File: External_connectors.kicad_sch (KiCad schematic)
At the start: 16 parts, among them CN1 JST_Battery, J11 CAN_TX, J12 CAN_RX, J13 Conn_01x08, J14 Conn_01x06, J15 Conn_01x10, J16 Conn_01x08, J2 A - B, J21 U2U, J3 H - L, J4 TYPE-C-31-M12_13, J5 EXT_LOAD, J9 Conn_01x06

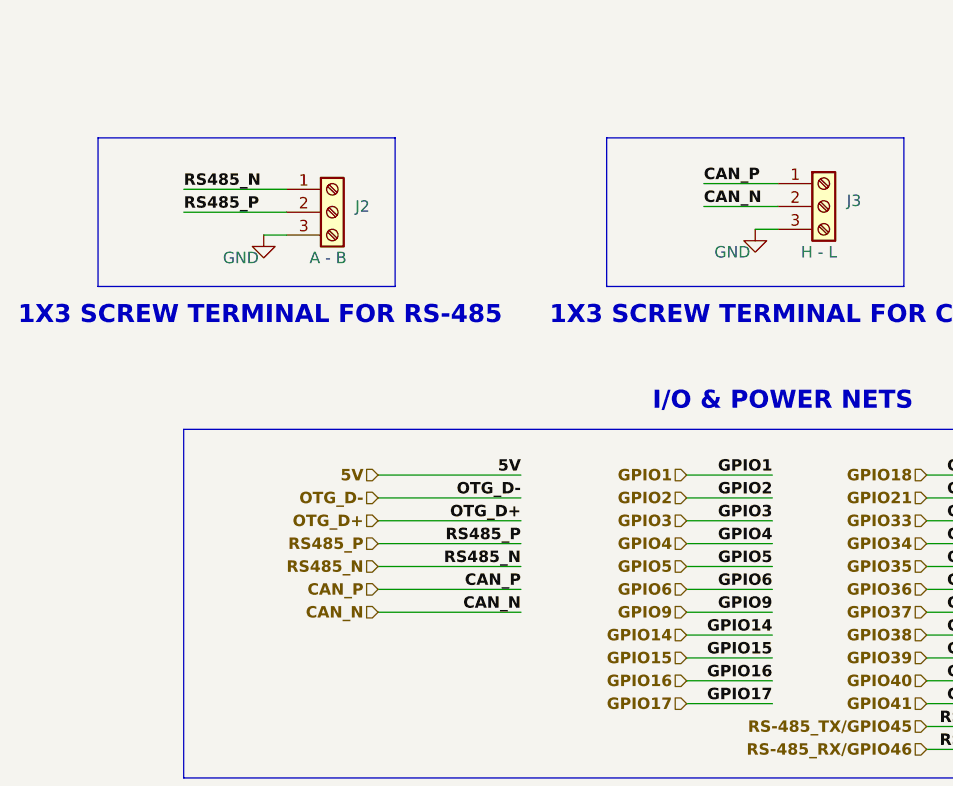
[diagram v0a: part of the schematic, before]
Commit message: Changed GPIO mapping
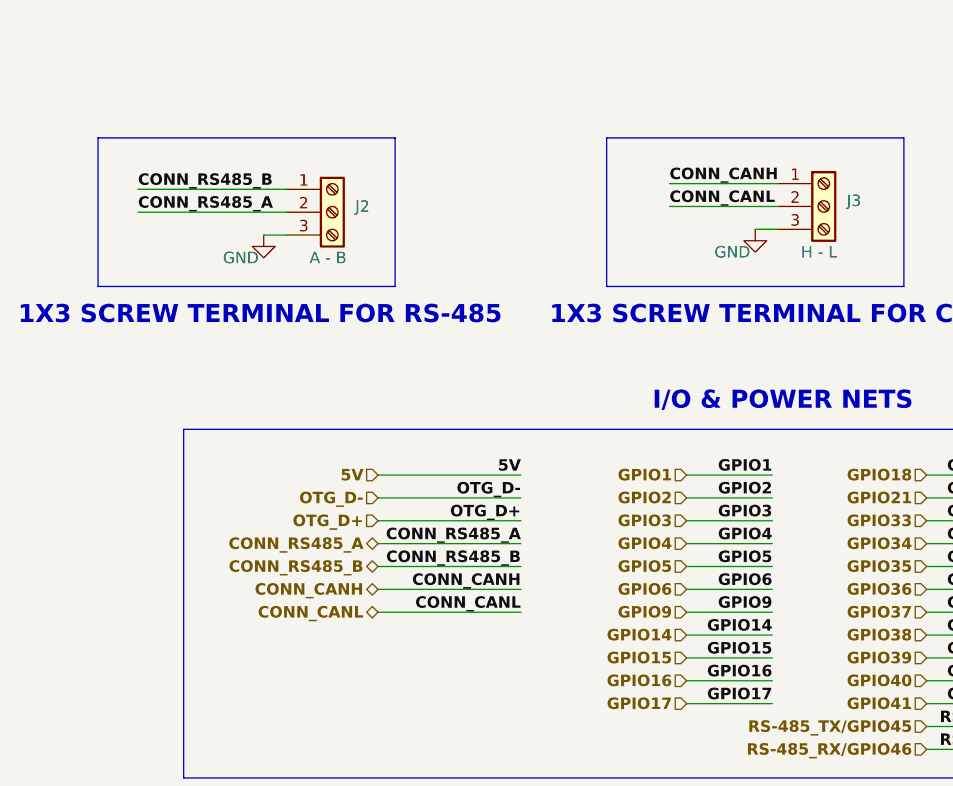
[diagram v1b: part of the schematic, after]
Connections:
- net CAN_N renamed CONN_CANL
- net CAN_P renamed CONN_CANH
- net RS485_N renamed CONN_RS485_B
- net RS485_P renamed CONN_RS485_A
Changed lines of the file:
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@@
     (stroke (width 1) (type default) (color 72 72 72 1))
   )
-  (wire (pts (xy 31.75 132.08) (xy 43.18 132.08))
+  (wire (pts (xy 26.67 132.08) (xy 43.18 132.08))
     (stroke (width 0) (type default))
   )
@@
     (stroke (width 0) (type default))
   )
-  (wire (pts (xy 31.75 129.54) (xy 43.18 129.54))
+  (wire (pts (xy 26.67 129.54) (xy 43.18 129.54))
     (stroke (width 0) (type default))
   )
@@
     (stroke (width 0) (type default))
   )
-  (wire (pts (xy 89.535 128.905) (xy 97.79 128.905))
+  (wire (pts (xy 85.725 128.905) (xy 97.79 128.905))
     (stroke (width 0) (type default))
   )
@@
     (stroke (width 0) (type default))
   )
-  (wire (pts (xy 89.535 131.445) (xy 97.79 131.445))
+  (wire (pts (xy 85.725 131.445) (xy 97.79 131.445))
     (stroke (width 0) (type default))
   )
@@
     (effects (font (size 1.27 1.27) bold (color 72 0 0 1)) (justify right bottom))
   )
-  (label "CAN_P" (at 89.535 128.905 0) (fields_autoplaced)
-    (effects (font (size 1.27 1.27) bold (color 0 0 0 1)) (justify left bottom))
-  )
   (label "V_BAT" (at 250.19 92.075 0) (fields_autoplaced)
     (effects (font (size 1.27 1.27) bold (color 132 132 0 1)) (justify left bottom))
@@
     (effects (font (size 1.27 1.27) bold (color 0 0 255 1)) (justify left bottom))
   )
-  (label "RS485_N" (at 69.215 171.45 180) (fields_autoplaced)
-    (effects (font (size 1.27 1.27) bold (color 0 0 0 1)) (justify right bottom))
-  )
   (label "GPIO4" (at 127 76.835 0) (fields_autoplaced)
     (effects (font (size 1.27 1.27) bold (color 72 0 0 1)) (justify left bottom))
@@
     (effects (font (size 1.27 1.27) bold (color 0 0 255 1)) (justify left bottom))
   )
-  (label "RS485_P" (at 31.75 132.08 0) (fields_autoplaced)
+  (label "CONN_RS485_A" (at 26.67 132.08 0) (fields_autoplaced)
     (effects (font (size 1.27 1.27) bold (color 0 0 0 1)) (justify left bottom))
   )
@@
     (effects (font (size 1.27 1.27) (thickness 0.254) bold (color 0 0 255 1)) (justify left bottom))
   )
-  (label "CAN_P" (at 69.215 173.99 180) (fields_autoplaced)
+  (label "CONN_CANH" (at 69.215 173.99 180) (fields_autoplaced)
     (effects (font (size 1.27 1.27) bold (color 0 0 0 1)) (justify right bottom))
   )
@@
     (effects (font (size 1.27 1.27) bold (color 0 194 0 1)) (justify right bottom))
   )
-  (label "RS485_P" (at 69.215 168.91 180) (fields_autoplaced)
-    (effects (font (size 1.27 1.27) bold (color 0 0 0 1)) (justify right bottom))
-  )
   (label "GPIO16" (at 97.155 184.15 180) (fields_autoplaced)
     (effects (font (size 1.27 1.27) bold (color 72 0 0 1)) (justify right bottom))
@@
     (effects (font (size 1.27 1.27) bold (color 72 0 0 1)) (justify left bottom))
   )
-  (label "CAN_N" (at 89.535 131.445 0) (fields_autoplaced)
-    (effects (font (size 1.27 1.27) bold (color 0 0 0 1)) (justify left bottom))
-  )
   (label "GPIO2" (at 97.155 163.83 180) (fields_autoplaced)
     (effects (font (size 1.27 1.27) bold (color 72 0 0 1)) (justify right bottom))
@@
     (effects (font (size 1.27 1.27) bold (color 72 0 0 1)) (justify right bottom))
   )
+  (label "CONN_RS485_A" (at 69.215 168.91 180) (fields_autoplaced)
+    (effects (font (size 1.27 1.27) bold (color 0 0 0 1)) (justify right bottom))
+  )
   (label "CC2" (at 86.36 62.865 0) (fields_autoplaced)
     (effects (font (size 1.27 1.27) bold (color 0 0 255 1)) (justify left bottom))
@@
     (effects (font (size 1.27 1.27) bold (color 72 0 0 1)) (justify right bottom))
   )
-  (label "CAN_N" (at 69.215 176.53 180) (fields_autoplaced)
+  (label "CONN_CANL" (at 69.215 176.53 180) (fields_autoplaced)
     (effects (font (size 1.27 1.27) bold (color 0 0 0 1)) (justify right bottom))
   )
@@
     (effects (font (size 1.27 1.27) bold (color 72 0 0 1)) (justify right bottom))
   )
-  (label "RS485_N" (at 31.75 129.54 0) (fields_autoplaced)
+  (label "CONN_RS485_B" (at 26.67 129.54 0) (fields_autoplaced)
     (effects (font (size 1.27 1.27) bold (color 0 0 0 1)) (justify left bottom))
   )
@@
     (effects (font (size 1.27 1.27) bold (color 132 132 0 1)) (justify right bottom))
   )
+  (label "CONN_CANH" (at 85.725 128.905 0) (fields_autoplaced)
+    (effects (font (size 1.27 1.27) bold (color 0 0 0 1)) (justify left bottom))
+  )
   (label "3V3" (at 127 48.895 0) (fields_autoplaced)
     (effects (font (size 1.27 1.27) bold (color 255 0 0 1)) (justify left bottom))
@@
     (effects (font (size 1.27 1.27) bold (color 72 0 0 1)) (justify right bottom))
   )
+  (label "CONN_CANL" (at 85.725 131.445 0) (fields_autoplaced)
+    (effects (font (size 1.27 1.27) bold (color 0 0 0 1)) (justify left bottom))
+  )
   (label "RS-485_TX{slash}GPIO46" (at 133.985 191.77 180) (fields_autoplaced)
     (effects (font (size 1.27 1.27) bold (color 0 0 255 1)) (justify right bottom))
@@
     (effects (font (size 1.27 1.27) bold (color 72 0 0 1)) (justify right bottom))
   )
+  (label "CONN_RS485_B" (at 69.215 171.45 180) (fields_autoplaced)
+    (effects (font (size 1.27 1.27) bold (color 0 0 0 1)) (justify right bottom))
+  )
   (label "GPIO36" (at 197.485 74.295 180) (fields_autoplaced)
     (effects (font (size 1.27 1.27) bold (color 72 0 0 1)) (justify right bottom))
@@
     (effects (font (size 1.27 1.27) (thickness 0.254) bold (color 72 0 72 1)) (justify right))
   )
-  (hierarchical_label "CAN_N" (shape input) (at 53.34 176.53 180) (fields_autoplaced)
+  (hierarchical_label "CONN_CANL" (shape bidirectional) (at 53.34 176.53 180) (fields_autoplaced)
     (effects (font (size 1.27 1.27) bold (color 0 0 0 1)) (justify right))
   )
@@
     (effects (font (size 1.27 1.27) (thickness 0.254) bold (color 72 0 72 1)) (justify right))
   )
-  (hierarchical_label "RS485_P" (shape input) (at 53.34 168.91 180) (fields_autoplaced)
+  (hierarchical_label "CONN_RS485_A" (shape bidirectional) (at 53.34 168.91 180) (fields_autoplaced)
     (effects (font (size 1.27 1.27) bold (color 0 0 0 1)) (justify right))
   )
@@
     (effects (font (size 1.27 1.27) (thickness 0.254) bold (color 132 132 0 1)) (justify right))
   )
-  (hierarchical_label "RS485_N" (shape input) (at 53.34 171.45 180) (fields_autoplaced)
+  (hierarchical_label "CONN_RS485_B" (shape bidirectional) (at 53.34 171.45 180) (fields_autoplaced)
     (effects (font (size 1.27 1.27) bold (color 0 0 0 1)) (justify right))
   )
@@
     (effects (font (size 1.27 1.27) (thickness 0.254) bold (color 0 0 255 1)) (justify right))
   )
-  (hierarchical_label "CAN_P" (shape input) (at 53.34 173.99 180) (fields_autoplaced)
+  (hierarchical_label "CONN_CANH" (shape bidirectional) (at 53.34 173.99 180) (fields_autoplaced)
     (effects (font (size 1.27 1.27) bold (color 0 0 0 1)) (justify right))
   )

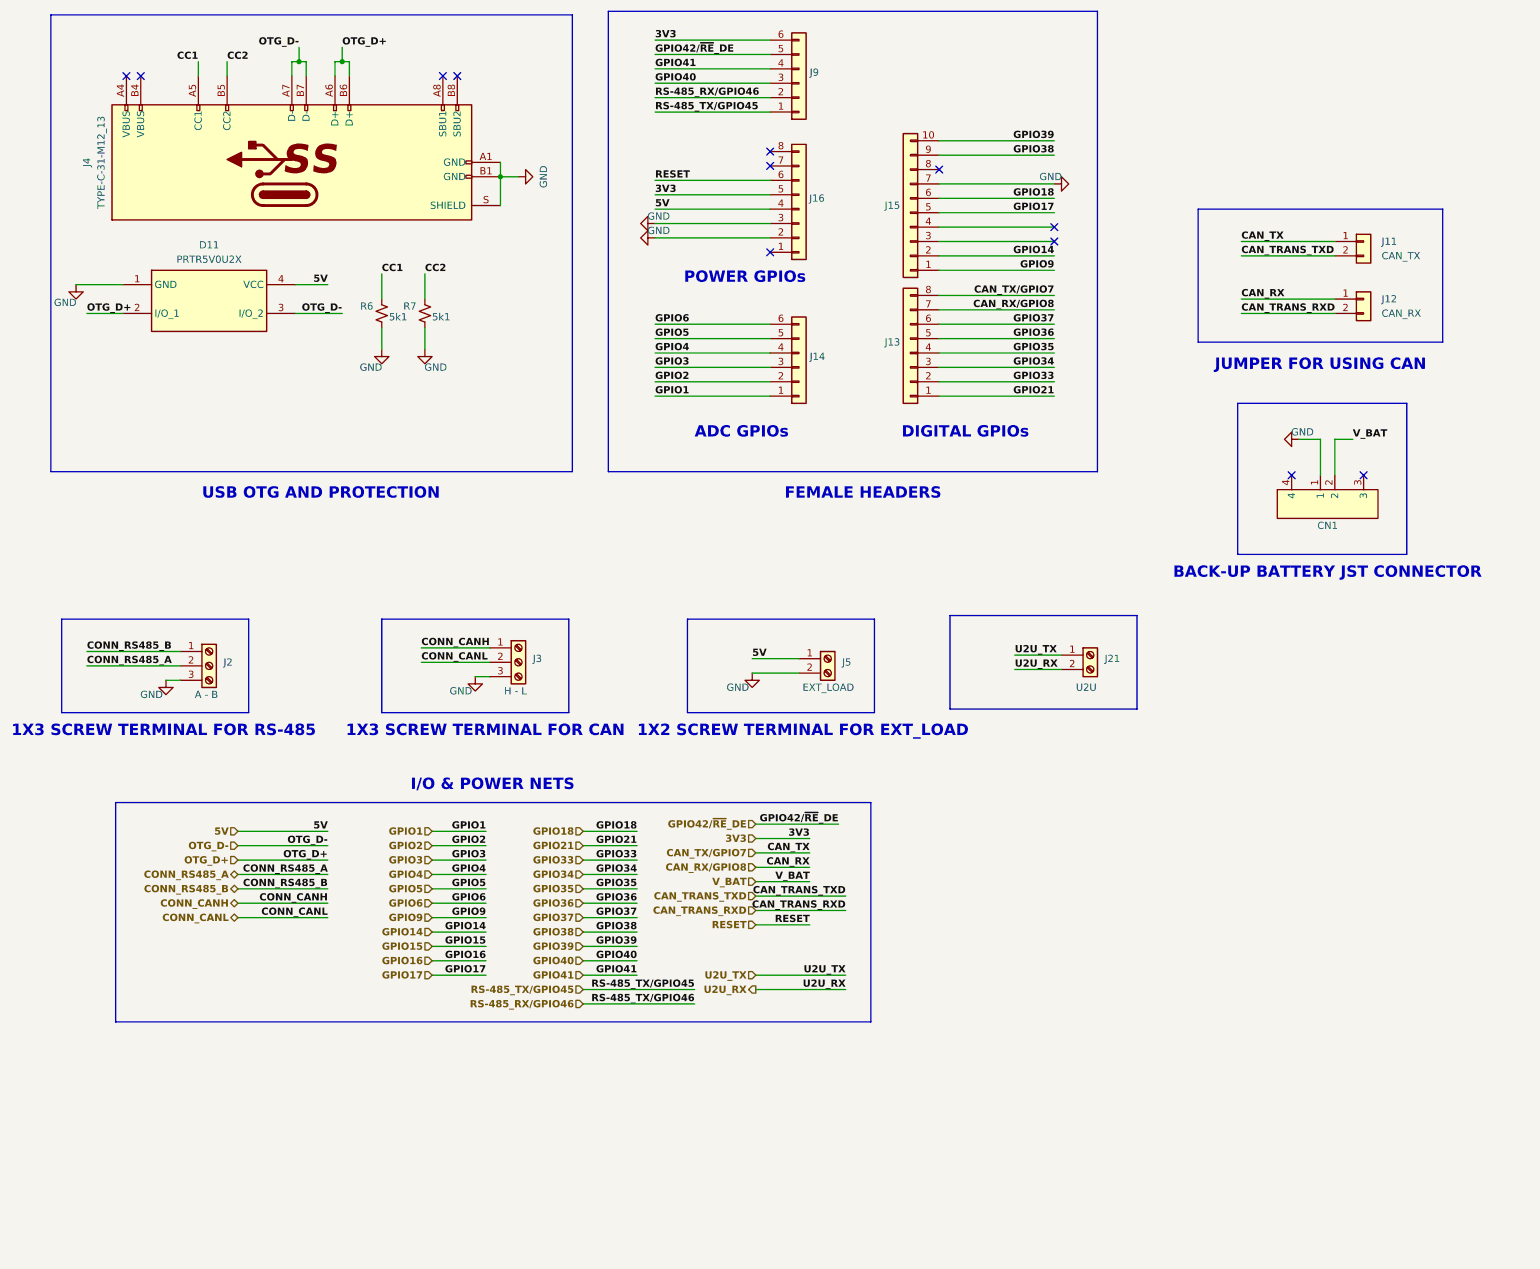
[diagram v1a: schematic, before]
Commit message: Changed MCU pin mapping
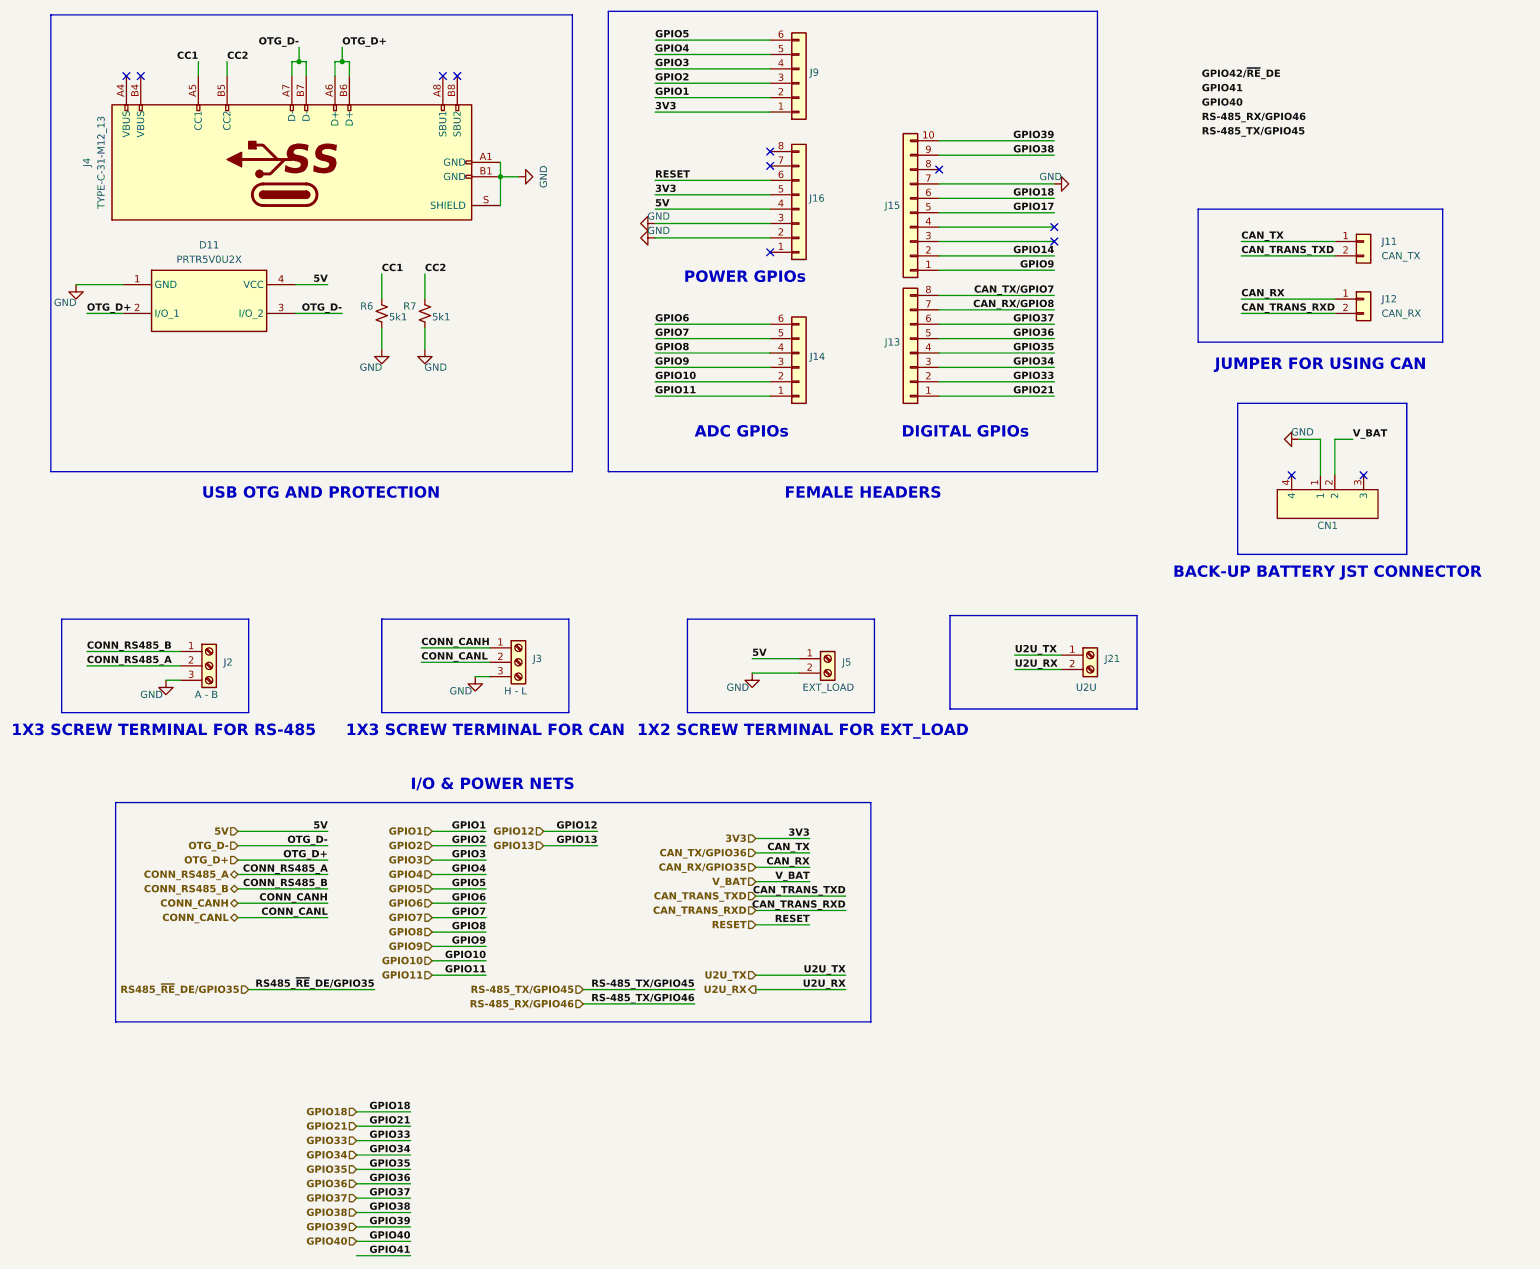
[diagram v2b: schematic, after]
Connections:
- net 3V3: now also J9.1 (Pin_1); no longer J9.6 (Pin_6)
- net CAN_RX/GPIO8: no longer J12.1 (Pin_1)
- net CAN_TX/GPIO7: no longer J11.1 (Pin_1)
- net GPIO1: now also J9.2 (Pin_2); no longer J14.1 (Pin_1)
- net GPIO2: now also J9.3 (Pin_3); no longer J14.2 (Pin_2)
- net GPIO3: now also J9.4 (Pin_4); no longer J14.3 (Pin_3)
- net GPIO4: now also J9.5 (Pin_5); no longer J14.4 (Pin_4)
- net GPIO40: no longer J9.3 (Pin_3)
- net GPIO41: no longer J9.4 (Pin_4)
- net GPIO42/~{RE}_DE: no longer J9.5 (Pin_5)
- net GPIO5: now also J9.6 (Pin_6); no longer J14.5 (Pin_5)
- net GPIO9: now also J14.3 (Pin_3)
- net RS-485_RX/GPIO46: no longer J9.2 (Pin_2)
- net RS-485_TX/GPIO45: no longer J9.1 (Pin_1)
- new net CAN_RX/GPIO35: J12.1 (Pin_1)
- new net CAN_TX/GPIO36: J11.1 (Pin_1)
- new net GPIO10: J14.2 (Pin_2)
- new net GPIO11: J14.1 (Pin_1)
- new net GPIO7: J14.5 (Pin_5)
- new net GPIO8: J14.4 (Pin_4)
